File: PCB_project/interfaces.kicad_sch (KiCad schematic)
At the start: 6 parts, among them J4 USB_C_Receptacle_USB2.0, U11 USBLC6-2SC6-ES

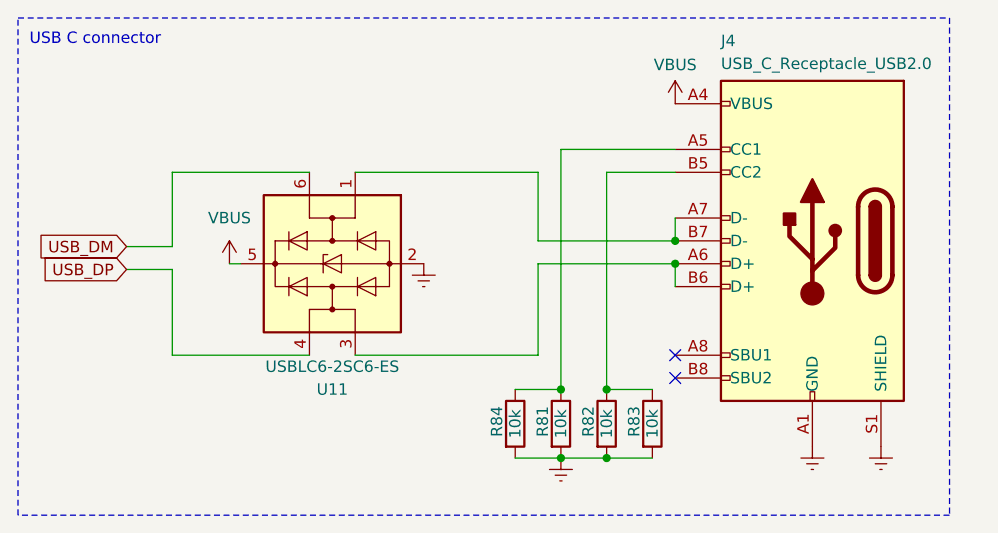
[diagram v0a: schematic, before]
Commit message: Almost ready version. Require more GND vias etc
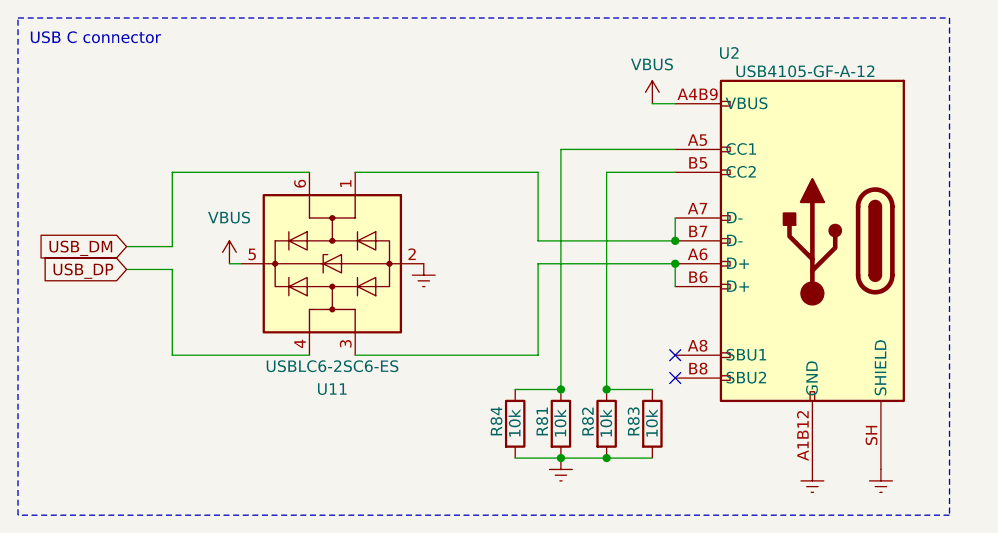
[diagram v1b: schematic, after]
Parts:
- removed J4: USB_C_Receptacle_USB2.0, KP-PTR_lib:USB_C_213716, symbol Connector:USB_C_Receptacle_USB2.0
- added U2: USB4105-GF-A-12, KP-PTR_lib:USB_C_16P_SMD_USB4105-GF-A, symbol KP-PTR_lib:USB_C_12P
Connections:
- net Earth: now also U2.A1B12 (GND), U2.B1A12 (GND), U2.SH (SHIELD)
- net VBUS: now also U2.A4B9 (VBUS), U2.B4A9 (VBUS)
- net at R81.1, R84.1: now also U2.A5 (CC1)
- net at U11.1 (I/O1): now also U2.A7 (D-), U2.B7 (D-)
- net at U11.3 (I/O2): now also U2.A6 (D+), U2.B6 (D+)
- net at R82.1, R83.1: now also U2.B5 (CC2)
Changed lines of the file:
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@@
+	)
+	(junction
+		(at 91.44 44.45)
+		(diameter 0)
+		(color 0 0 0 0)
+	)
+	(junction
+		(at 78.74 58.42)
+		(diameter 0)
+		(color 0 0 0 0)
+	)
+	(junction
+		(at 78.74 66.04)
+		(diameter 0)
+		(color 0 0 0 0)
 	)
 	(junction
@@
 	)
 	(junction
-		(at 78.74 58.42)
-		(diameter 0)
-		(color 0 0 0 0)
-	)
-	(junction
-		(at 78.74 66.04)
-		(diameter 0)
-		(color 0 0 0 0)
-	)
-	(junction
-		(at 91.44 44.45)
-		(diameter 0)
-		(color 0 0 0 0)
-	)
-	(junction
 		(at 83.82 58.42)
 		(diameter 0)
@@
 		(pts
 			(xy 55.88 34.29) (xy 76.2 34.29)
+		)
+		(stroke
+			(width 0)
+			(type default)
+		)
+	)
+	(wire
+		(pts
+			(xy 88.9 26.67) (xy 91.44 26.67)
 		)
 		(stroke
@@
 	(symbol
 		(lib_id "power:VBUS")
-		(at 91.44 26.67 0)
+		(at 88.9 26.67 0)
 		(unit 1)
 		(body_style 1)
@@
 		(dnp no)
 		(property "Reference" "#PWR0126"
-			(at 91.44 30.48 0)
+			(at 88.9 30.48 0)
 			(hide yes)
 			(show_name no)
@@
 		)
 		(property "Value" "VBUS"
-			(at 91.44 22.352 0)
+			(at 88.9 22.352 0)
 			(show_name no)
 			(do_not_autoplace no)
@@
 		)
 		(property "Footprint" ""
-			(at 91.44 26.67 0)
+			(at 88.9 26.67 0)
 			(hide yes)
 			(show_name no)
@@
 		)
 		(property "Datasheet" ""
-			(at 91.44 26.67 0)
+			(at 88.9 26.67 0)
 			(hide yes)
 			(show_name no)
@@
 		)
 		(property "Description" ""
-			(at 91.44 26.67 0)
+			(at 88.9 26.67 0)
 			(show_name no)
 			(do_not_autoplace no)
@@
 	(symbol
 		(lib_id "power:Earth")
-		(at 114.3 64.77 0)
+		(at 114.3 67.31 0)
 		(unit 1)
 		(body_style 1)
@@
 		(fields_autoplaced yes)
 		(property "Reference" "#PWR0138"
+			(at 114.3 73.66 0)
+			(hide yes)
+			(show_name no)
+			(do_not_autoplace no)
+			(effects
+				(font
+					(size 1.27 1.27)
+				)
+			)
+		)
+		(property "Value" "Earth"
 			(at 114.3 71.12 0)
 			(hide yes)
@@
 			)
 		)
-		(property "Value" "Earth"
-			(at 114.3 68.58 0)
-			(hide yes)
-			(show_name no)
-			(do_not_autoplace no)
-			(effects
-				(font
-					(size 1.27 1.27)
-				)
-			)
-		)
 		(property "Footprint" ""
-			(at 114.3 64.77 0)
+			(at 114.3 67.31 0)
 			(hide yes)
 			(show_name no)
@@
 		)
 		(property "Datasheet" ""
-			(at 114.3 64.77 0)
+			(at 114.3 67.31 0)
 			(hide yes)
 			(show_name no)
@@
 		)
 		(property "Description" ""
-			(at 114.3 64.77 0)
+			(at 114.3 67.31 0)
 			(show_name no)
 			(do_not_autoplace no)
@@
 	(symbol
 		(lib_id "power:Earth")
-		(at 106.68 64.77 0)
+		(at 106.68 67.31 0)
 		(unit 1)
 		(body_style 1)
@@
 		(fields_autoplaced yes)
 		(property "Reference" "#PWR0137"
+			(at 106.68 73.66 0)
+			(hide yes)
+			(show_name no)
+			(do_not_autoplace no)
+			(effects
+				(font
+					(size 1.27 1.27)
+				)
+			)
+		)
+		(property "Value" "Earth"
 			(at 106.68 71.12 0)
 			(hide yes)
@@
 			)
 		)
-		(property "Value" "Earth"
-			(at 106.68 68.58 0)
-			(hide yes)
-			(show_name no)
-			(do_not_autoplace no)
-			(effects
-				(font
-					(size 1.27 1.27)
-				)
-			)
-		)
 		(property "Footprint" ""
-			(at 106.68 64.77 0)
+			(at 106.68 67.31 0)
 			(hide yes)
 			(show_name no)
@@
 		)
 		(property "Datasheet" ""
-			(at 106.68 64.77 0)
+			(at 106.68 67.31 0)
 			(hide yes)
 			(show_name no)
@@
 		)
 		(property "Description" ""
-			(at 106.68 64.77 0)
+			(at 106.68 67.31 0)
 			(show_name no)
 			(do_not_autoplace no)
@@
 	)
 	(symbol
-		(lib_id "Connector:USB_C_Receptacle_USB2.0")
-		(at 106.68 41.91 0)
-		(mirror y)
+		(lib_id "KP-PTR_lib:USB_C_12P")
+		(at 107.95 44.45 0)
 		(unit 1)
 		(body_style 1)
@@
 		(in_pos_files yes)
 		(dnp no)
-		(property "Reference" "J4"
-			(at 96.52 19.685 0)
-			(show_name no)
-			(do_not_autoplace no)
-			(effects
-				(font
-					(size 1.27 1.27)
-				)
-				(justify right)
-			)
-		)
-		(property "Value" "USB_C_Receptacle_USB2.0"
-			(at 96.52 22.225 0)
-			(show_name no)
-			(do_not_autoplace no)
-			(effects
-				(font
-					(size 1.27 1.27)
-				)
-				(justify right)
-			)
-		)
-		(property "Footprint" "KP-PTR_lib:USB_C_213716"
-			(at 102.87 41.91 0)
-			(hide yes)
-			(show_name no)
-			(do_not_autoplace no)
-			(effects
-				(font
-					(size 1.27 1.27)
-				)
-			)
-		)
-		(property "Datasheet" "https://www.usb.org/sites/default/files/documents/usb_type-c.zip"
-			(at 102.87 41.91 0)
+		(property "Reference" "U2"
+			(at 96.266 21.082 0)
+			(show_name no)
+			(do_not_autoplace no)
+			(effects
+				(font
+					(size 1.27 1.27)
+				)
+				(justify left)
+			)
+		)
+		(property "Value" "USB4105-GF-A-12"
+			(at 105.918 23.114 0)
+			(show_name no)
+			(do_not_autoplace no)
+			(effects
+				(font
+					(size 1.27 1.27)
+				)
+			)
+		)
+		(property "Footprint" "KP-PTR_lib:USB_C_16P_SMD_USB4105-GF-A"
+			(at 107.95 44.45 0)
+			(hide yes)
+			(show_name no)
+			(do_not_autoplace no)
+			(effects
+				(font
+					(size 1.27 1.27)
+				)
+			)
+		)
+		(property "Datasheet" ""
+			(at 107.95 44.45 0)
 			(hide yes)
 			(show_name no)
@@
 		)
 		(property "Description" ""
-			(at 106.68 41.91 0)
-			(show_name no)
-			(do_not_autoplace no)
-			(effects
-				(font
-					(size 1.27 1.27)
-				)
-			)
-		)
-		(pin "A1"
-		)
-		(pin "A12"
-		)
-		(pin "A4"
+			(at 107.95 44.45 0)
+			(hide yes)
+			(show_name no)
+			(do_not_autoplace no)
+			(effects
+				(font
+					(size 1.27 1.27)
+				)
+			)
+		)
+		(pin "A1B12"
 		)
 		(pin "A5"
@@
 		(pin "A7"
 		)
+		(pin "B4A9"
+		)
+		(pin "A4B9"
+		)
+		(pin "B5"
+		)
 		(pin "A8"
 		)
-		(pin "A9"
-		)
-		(pin "B1"
-		)
-		(pin "B12"
-		)
-		(pin "B4"
-		)
-		(pin "B5"
-		)
 		(pin "B6"
 		)
+		(pin "B1A12"
+		)
+		(pin "B8"
+		)
 		(pin "B7"
 		)
-		(pin "B8"
-		)
-		(pin "B9"
-		)
-		(pin "S1"
+		(pin "SH"
 		)
 		(instances
 			(project "kp-ptr"
 				(path "/9538e4ed-27e6-4c37-b989-9859dc0d49e8/5f9da060-2eb0-4ae6-ad5b-b0da419a62a6"
-					(reference "J4")
+					(reference "U2")
 					(unit 1)
 				)
